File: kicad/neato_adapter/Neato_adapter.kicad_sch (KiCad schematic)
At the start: 7 parts, among them J1 JST PH B4B Vert, J2 JST PH B2B Vert, J3 JST PH B4B Vert, Q1 AS2302, U1 DNP LM2596

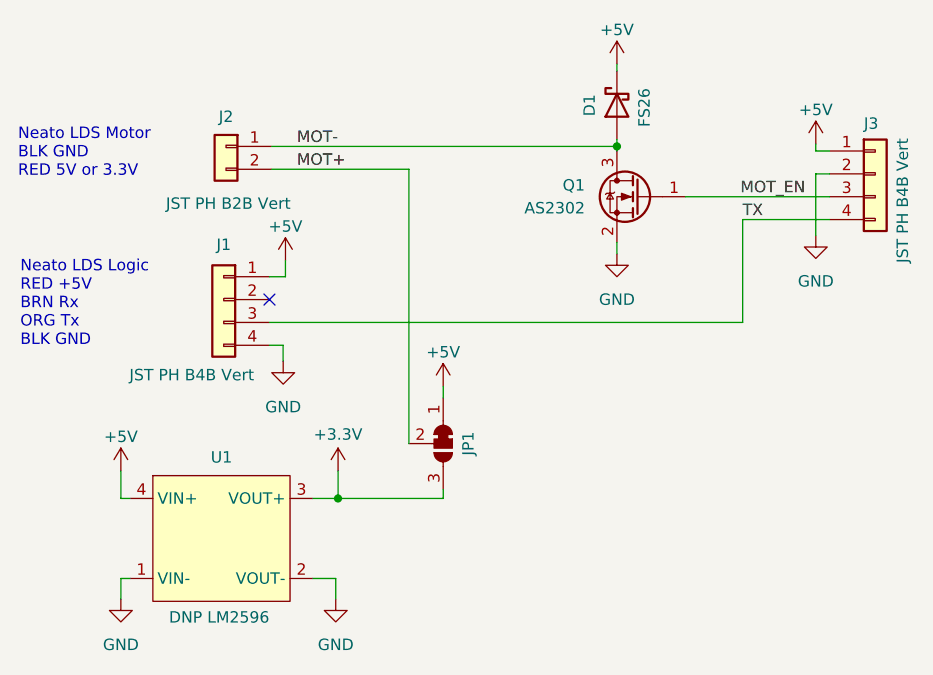
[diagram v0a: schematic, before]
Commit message: Neato adapter PCB Gerber
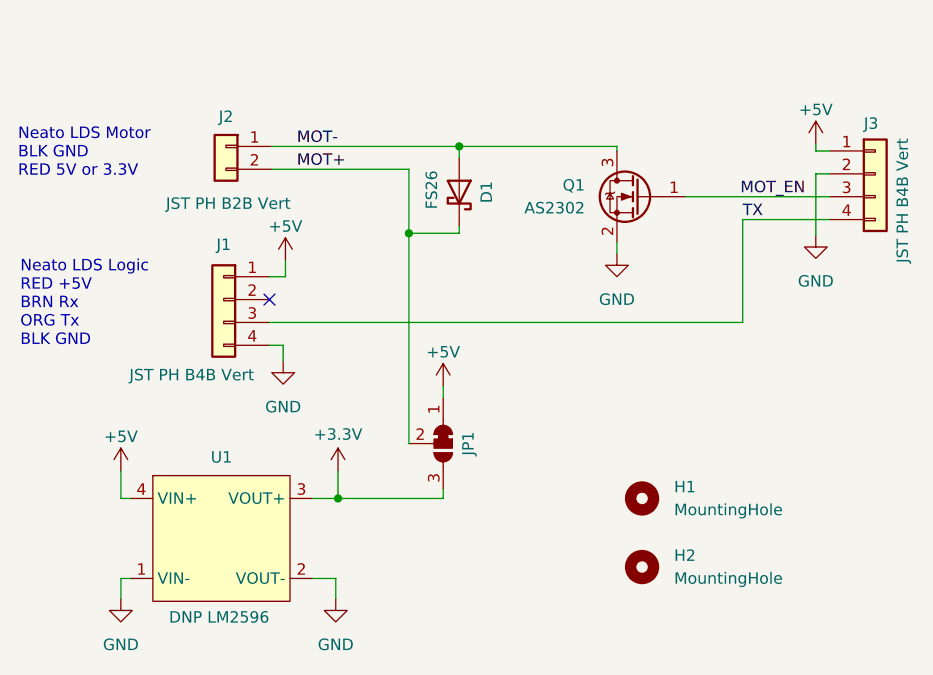
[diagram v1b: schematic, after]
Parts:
- added H1, H2: MountingHole, MountingHole:MountingHole_3.2mm_M3, symbol Mechanical:MountingHole
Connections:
- net +5V: no longer D1.1 (K)
- net MOT+: now also D1.1 (K)
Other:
- moved on the sheet: D1
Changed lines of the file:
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@@
     (company "makerspet.com")
   )
-  (junction (at 110.49 34.798) (diameter 0) (color 0 0 0 0)
-  )
   (junction (at 79.502 73.914) (diameter 0) (color 0 0 0 0)
+  )
+  (junction (at 92.964 34.798) (diameter 0) (color 0 0 0 0)
+  )
+  (junction (at 87.376 44.45) (diameter 0) (color 0 0 0 0)
   )
   (no_connect (at 71.882 51.816))
@@
     (stroke (width 0) (type default))
   )
-  (wire (pts (xy 72.136 34.798) (xy 110.49 34.798))
+  (wire (pts (xy 72.136 34.798) (xy 92.964 34.798))
     (stroke (width 0) (type default))
   )
@@
     (stroke (width 0) (type default))
   )
-  (wire (pts (xy 87.376 67.818) (xy 87.376 37.338))
+  (wire (pts (xy 87.376 67.818) (xy 87.376 44.45))
     (stroke (width 0) (type default))
   )
@@
     (stroke (width 0) (type default))
   )
-  (wire (pts (xy 110.49 34.036) (xy 110.49 34.798))
+  (wire (pts (xy 92.964 34.798) (xy 110.49 34.798))
+    (stroke (width 0) (type default))
+  )
+  (wire (pts (xy 87.376 44.45) (xy 87.376 37.338))
     (stroke (width 0) (type default))
   )
@@
     (stroke (width 0) (type default))
   )
+  (wire (pts (xy 92.964 43.688) (xy 92.964 44.45))
+    (stroke (width 0) (type default))
+  )
   (wire (pts (xy 118.11 40.386) (xy 134.112 40.386))
     (stroke (width 0) (type default))
   )
+  (wire (pts (xy 92.964 44.45) (xy 87.376 44.45))
+    (stroke (width 0) (type default))
+  )
   (wire (pts (xy 79.248 82.804) (xy 76.708 82.804))
     (stroke (width 0) (type default))
@@
     (stroke (width 0) (type default))
   )
-  (wire (pts (xy 110.49 25.654) (xy 110.49 26.416))
-    (stroke (width 0) (type default))
-  )
   (wire (pts (xy 71.882 54.356) (xy 124.46 54.356))
+    (stroke (width 0) (type default))
+  )
+  (wire (pts (xy 92.964 34.798) (xy 92.964 36.068))
     (stroke (width 0) (type default))
   )
@@
     )
   )
-  (symbol (lib_id "power:+5V") (at 110.49 25.654 0) (unit 1)
-    (in_bom yes) (on_board yes) (dnp no) (fields_autoplaced)
-    (property "Reference" "#PWR01" (at 110.49 29.464 0)
-      (effects (font (size 1.27 1.27)) hide)
-    )
-    (property "Value" "+5V" (at 110.49 21.844 0)
-      (effects (font (size 1.27 1.27)))
-    )
-    (property "Footprint" "" (at 110.49 25.654 0)
-      (effects (font (size 1.27 1.27)) hide)
-    )
-    (property "Datasheet" "" (at 110.49 25.654 0)
-      (effects (font (size 1.27 1.27)) hide)
-    )
-    (pin "1")
-    (instances
-      (project "Neato_adapter"
-        (path "/c13da21a-388e-44a0-831a-aa3d56cf7c53"
-          (reference "#PWR01") (unit 1)
-        )
-      )
-      (project "esp32_breakout"
-        (path "/e24ae185-8f18-408c-aee8-f727519bade3"
-          (reference "#PWR012") (unit 1)
+  (symbol (lib_id "Mechanical:MountingHole") (at 113.284 81.534 0) (unit 1)
+    (in_bom no) (on_board yes) (dnp no) (fields_autoplaced)
+    (property "Reference" "H2" (at 116.84 80.264 0)
+      (effects (font (size 1.27 1.27)) (justify left))
+    )
+    (property "Value" "MountingHole" (at 116.84 82.804 0)
+      (effects (font (size 1.27 1.27)) (justify left))
+    )
+    (property "Footprint" "MountingHole:MountingHole_3.2mm_M3" (at 113.284 81.534 0)
+      (effects (font (size 1.27 1.27)) hide)
+    )
+    (property "Datasheet" "~" (at 113.284 81.534 0)
+      (effects (font (size 1.27 1.27)) hide)
+    )
+    (instances
+      (project "Neato_adapter"
+        (path "/c13da21a-388e-44a0-831a-aa3d56cf7c53"
+          (reference "H2") (unit 1)
         )
       )
@@
     )
   )
-  (symbol (lib_id "Device:D_Schottky") (at 110.49 30.226 90) (mirror x) (unit 1)
+  (symbol (lib_id "Device:D_Schottky") (at 92.964 39.878 270) (mirror x) (unit 1)
     (in_bom yes) (on_board yes) (dnp no)
-    (property "Reference" "D1" (at 107.442 30.226 0)
-      (effects (font (size 1.27 1.27)))
-    )
-    (property "Value" "FS26" (at 113.538 30.48 0)
-      (effects (font (size 1.27 1.27)))
-    )
-    (property "Footprint" "Diode_SMD:D_SOD-123F" (at 110.49 30.226 0)
-      (effects (font (size 1.27 1.27)) hide)
-    )
-    (property "Datasheet" "https://www.digikey.com/en/products/detail/good-ark-semiconductor/FS26/18667798" (at 110.49 30.226 0)
+    (property "Reference" "D1" (at 96.012 39.878 0)
+      (effects (font (size 1.27 1.27)))
+    )
+    (property "Value" "FS26" (at 89.916 39.624 0)
+      (effects (font (size 1.27 1.27)))
+    )
+    (property "Footprint" "Diode_SMD:D_SOD-123F" (at 92.964 39.878 0)
+      (effects (font (size 1.27 1.27)) hide)
+    )
+    (property "Datasheet" "https://www.digikey.com/en/products/detail/good-ark-semiconductor/FS26/18667798" (at 92.964 39.878 0)
       (effects (font (size 1.27 1.27)) hide)
     )
@@
         )
       )
+    )
+  )
+  (symbol (lib_id "Mechanical:MountingHole") (at 113.284 73.914 0) (unit 1)
+    (in_bom no) (on_board yes) (dnp no) (fields_autoplaced)
+    (property "Reference" "H1" (at 116.84 72.644 0)
+      (effects (font (size 1.27 1.27)) (justify left))
+    )
+    (property "Value" "MountingHole" (at 116.84 75.184 0)
+      (effects (font (size 1.27 1.27)) (justify left))
+    )
+    (property "Footprint" "MountingHole:MountingHole_3.2mm_M3" (at 113.284 73.914 0)
+      (effects (font (size 1.27 1.27)) hide)
+    )
+    (property "Datasheet" "~" (at 113.284 73.914 0)
+      (effects (font (size 1.27 1.27)) hide)
+    )
+    (instances
+      (project "Neato_adapter"
+        (path "/c13da21a-388e-44a0-831a-aa3d56cf7c53"
+          (reference "H1") (unit 1)
+        )
+      )
